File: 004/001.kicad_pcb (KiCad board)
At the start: 2 copper layers, 75 x 98.8 mm, 37 parts, among them J1 CONN_01X08, J2 CONN_01X08, U1 2019.All.Mask.02, U10 Holder.Cu.Mask.01, U11 logo.B.Mask.Der.01, U12 logo.B.Mask.Izq.01, U13 logo.F.Mask.Der.01, U14 logo.F.Mask.Izq.01, U15 MKR_Family, U2 2019.All.Mask.03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

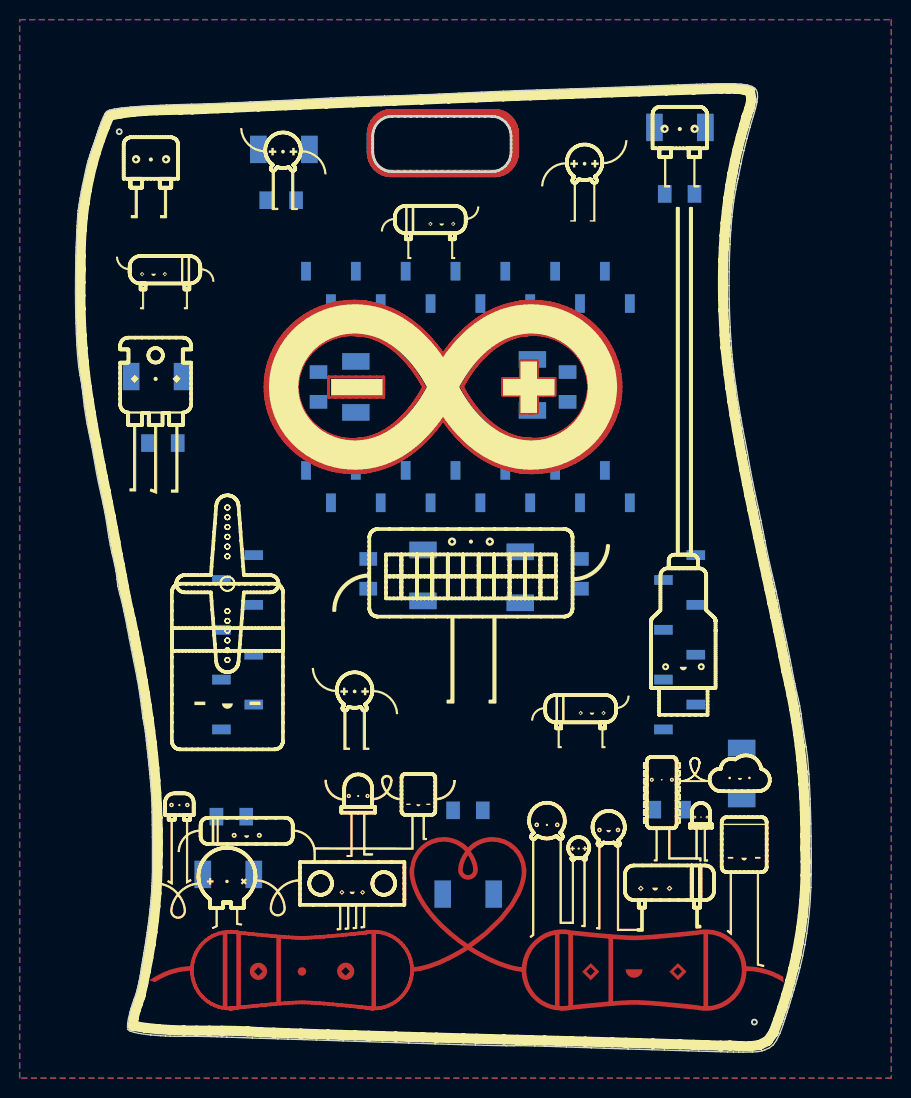
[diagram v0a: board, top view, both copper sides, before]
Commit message: Rooteo
Se rooteo la carpeta 004 coin dos versiones una a una capa y la otra en las dos, saludos! @antonio_raptors
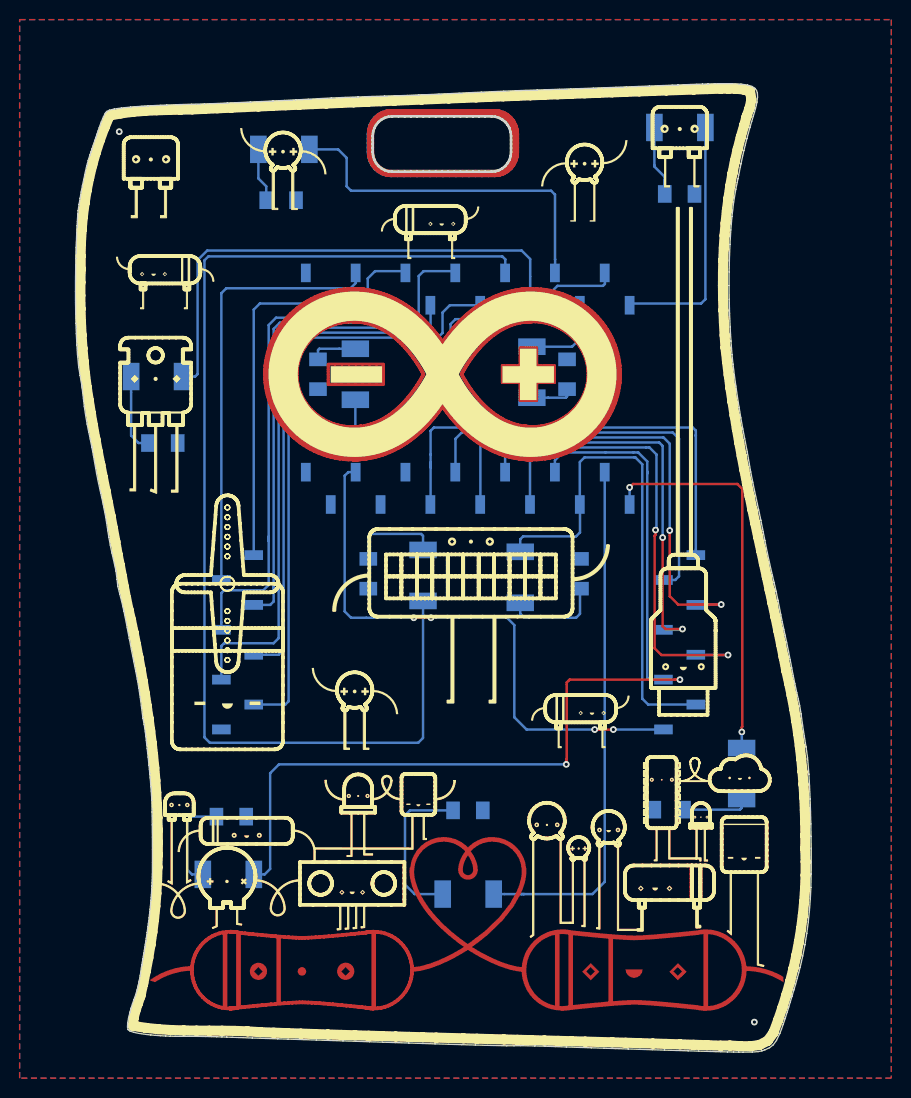
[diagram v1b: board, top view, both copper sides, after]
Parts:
- moved U14 1.30 mm to (130.0, 80.7)
- moved U3 1.30 mm to (138.4, 80.6)
- moved U6 1.30 mm to (138.4, 80.6)
- moved U7 1.30 mm to (138.4, 80.6)
- moved R5 1.30 mm to (125.7, 80.6)
- moved D5 1.30 mm to (129.5, 80.6)
- moved R4 1.30 mm to (151.1, 80.6)
- moved U13 1.30 mm to (146.6, 80.6)
- moved D4 1.30 mm to (147.5, 80.4)
- moved U11 1.30 mm to (146.8, 80.6)
- moved U12 1.30 mm to (130.0, 80.6)
- moved U8 1.30 mm to (138.3, 80.6)
- moved U15 0.18 mm to (140.9, 82.1)
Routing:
- net /D0: track 0.00 -> 117.5 mm
- net /D9-SCK: track 0.00 -> 99.8 mm, vias 0 -> 2
- net /A5: track 0.00 -> 64.2 mm
- net /A6: track 0.00 -> 62.6 mm
- net +3V3: track 0.00 -> 58.1 mm, vias 0 -> 4
- net /A3: track 0.00 -> 54.3 mm
- net /D7: track 0.00 -> 53.9 mm
- net /A4: track 0.00 -> 53.0 mm
- net /D1: track 0.00 -> 52.5 mm
- net /D8-MOSI: track 0.00 -> 51.5 mm
- net /D10-MISO: track 0.00 -> 49.6 mm, vias 0 -> 2
- net /D12-SCL: track 0.00 -> 49.6 mm, vias 0 -> 2
- net /D14<-TX: track 0.00 -> 48.0 mm
- net /A1: track 0.00 -> 44.6 mm
- net /A2: track 0.00 -> 43.7 mm
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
